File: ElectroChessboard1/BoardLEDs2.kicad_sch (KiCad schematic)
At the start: 35 parts, among them IC73 CD74HC154M96

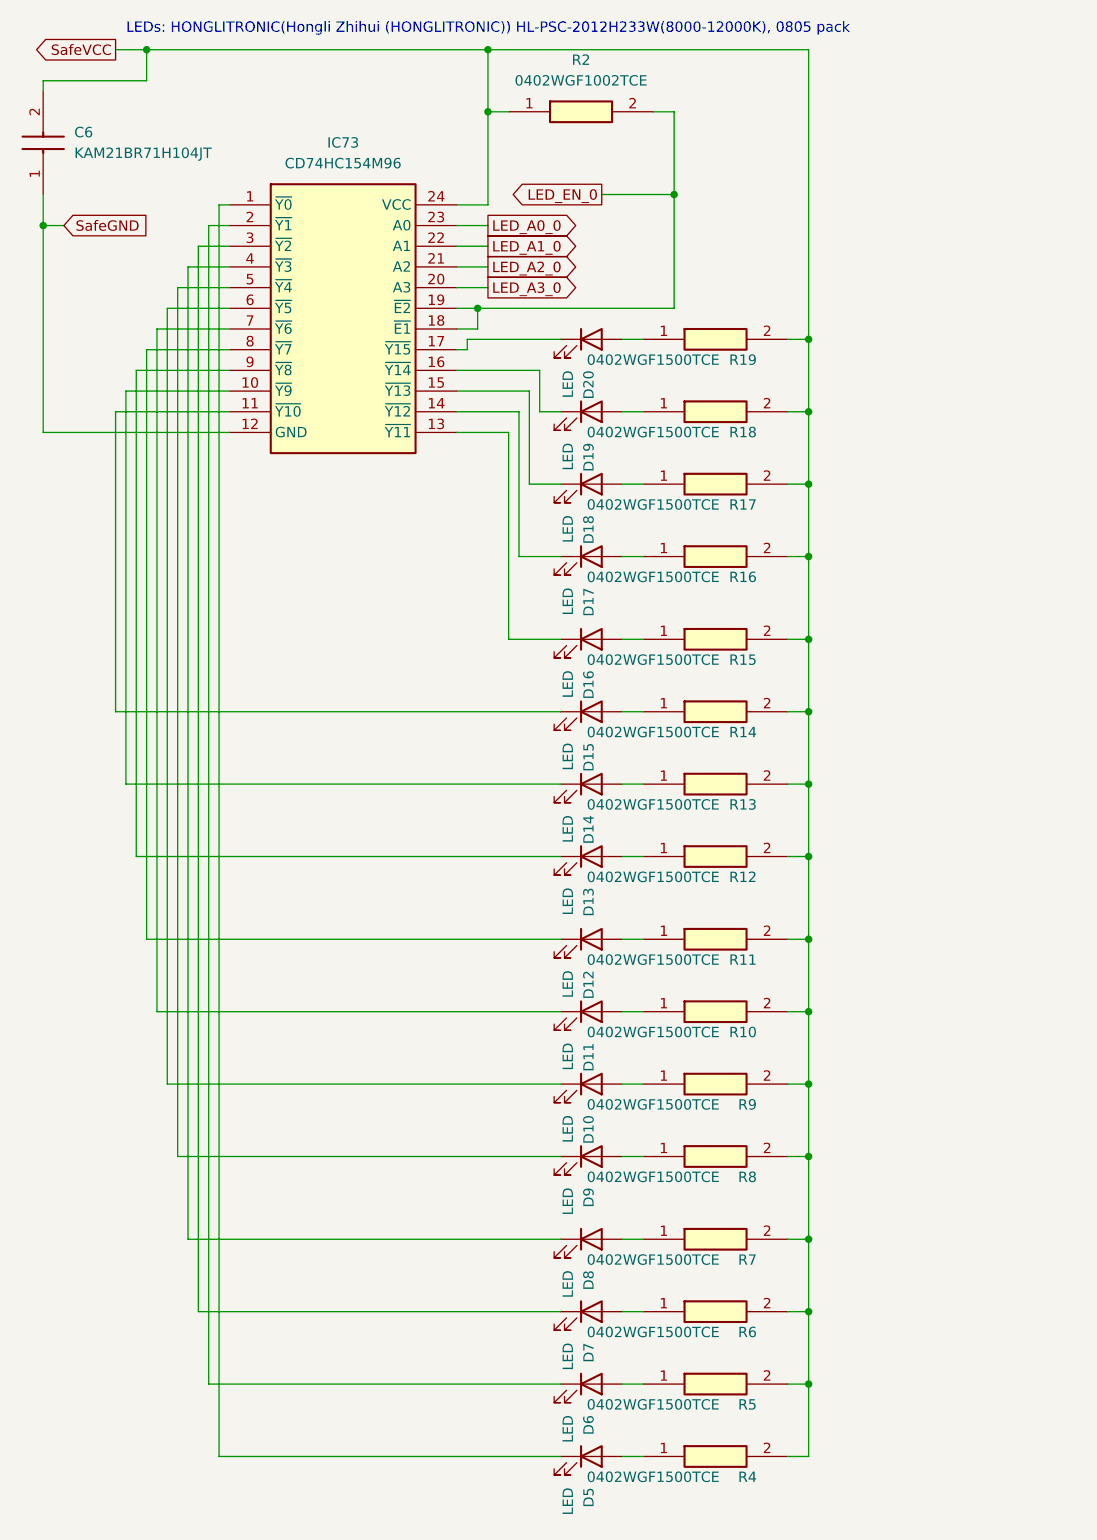
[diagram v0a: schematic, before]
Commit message: LEDs added
Wired Hall sensors and LEDs
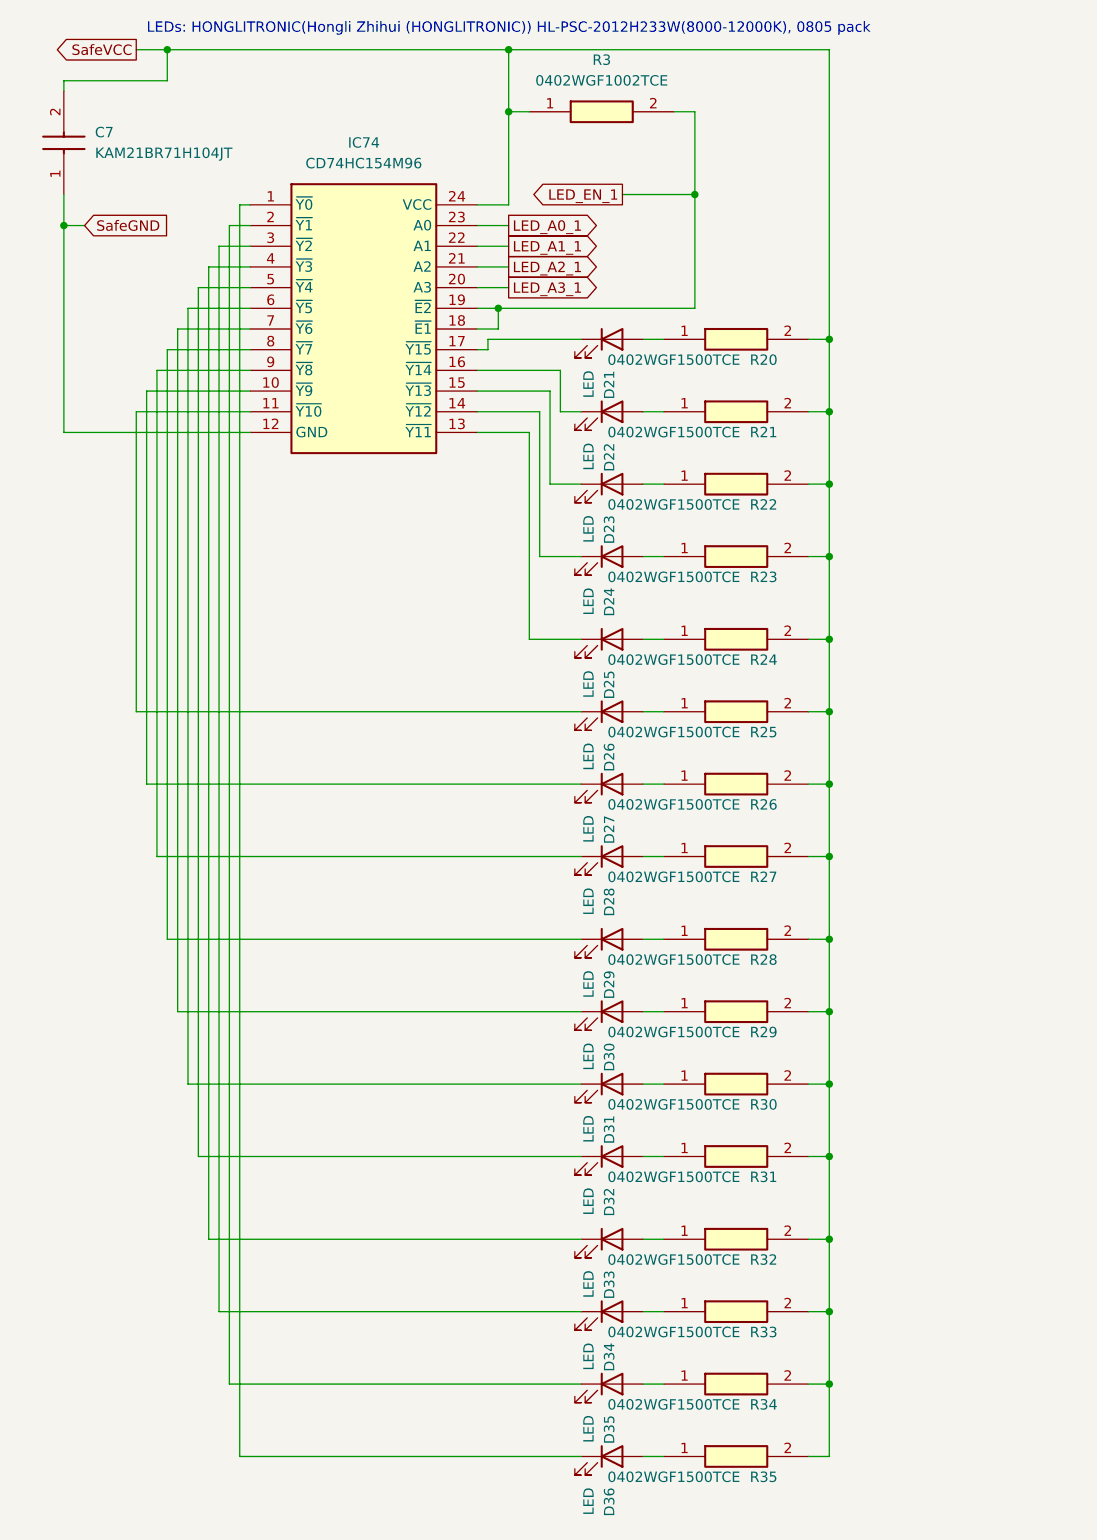
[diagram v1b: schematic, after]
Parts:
- removed C6: KAM21BR71H104JT, CAPC2012X94N, symbol SamacSys_Parts:KAM21BR71H104JT
- removed D10, D11, D12, D13, D14, D15, D16, D17, D18, D19, D20, D5, D6, D7, D8, D9: LED, LED_SMD:LED_0805_2012Metric, symbol Device:LED
- removed IC73: CD74HC154M96, SOIC127P1030X265-24N, symbol SamacSys_Parts:CD74HC154M96
- removed R10, R11, R12, R13, R14, R15, R16, R17, R18, R19, R4, R5, R6, R7, R8, R9: 0402WGF1500TCE, RESC1005X40N, symbol SamacSys_Parts:0402WGF1500TCE
- removed R2: 0402WGF1002TCE, RESC1005X40N, symbol SamacSys_Parts:0402WGF1002TCE
- added C7: KAM21BR71H104JT, CAPC2012X94N, symbol SamacSys_Parts:KAM21BR71H104JT
- added D21, D22, D23, D24, D25, D26, D27, D28, D29, D30, D31, D32, D33, D34, D35, D36: LED, LED_SMD:LED_0805_2012Metric, symbol Device:LED
- added IC74: CD74HC154M96, SOIC127P1030X265-24N, symbol SamacSys_Parts:CD74HC154M96
- added R20, R21, R22, R23, R24, R25, R26, R27, R28, R29, R30, R31, R32, R33, R34, R35: 0402WGF1500TCE, RESC1005X40N, symbol SamacSys_Parts:0402WGF1500TCE
- added R3: 0402WGF1002TCE, RESC1005X40N, symbol SamacSys_Parts:0402WGF1002TCE
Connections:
- net SafeGND: now also C7.1, IC74.12 (GND)
- net SafeVCC: now also C7.2, IC74.24 (VCC), R20.2, R21.2, R22.2, R23.2, R24.2, R25.2, R26.2, R27.2, R28.2, R29.2, R3.1, R30.2, R31.2, R32.2, R33.2, R34.2, R35.2
- new net: D22.1 (K), IC74.16 (~{Y14})
- new net: D22.2 (A), R21.1
- new net: D36.2 (A), R35.1
- new net: D35.2 (A), R34.1
- new net: D31.1 (K), IC74.6 (~{Y5})
- new net: D31.2 (A), R30.1
- new net: D29.1 (K), IC74.8 (~{Y7})
- new net: D29.2 (A), R28.1
- new net: D25.1 (K), IC74.13 (~{Y11})
- new net: D25.2 (A), R24.1
- new net: D21.2 (A), R20.1
- new net: D36.1 (K), IC74.1 (~{Y0})
- new net: D32.1 (K), IC74.5 (~{Y4})
- new net: D32.2 (A), R31.1
- new net: D33.2 (A), R32.1
- new net: D23.1 (K), IC74.15 (~{Y13})
- new net: D23.2 (A), R22.1
- new net: D26.2 (A), R25.1
- new net: D21.1 (K), IC74.17 (~{Y15})
- new net: D26.1 (K), IC74.11 (~{Y10})
- new net: D35.1 (K), IC74.2 (~{Y1})
- new net: D34.2 (A), R33.1
- new net: D28.2 (A), R27.1
- new net: D27.1 (K), IC74.10 (~{Y9})
- new net: D27.2 (A), R26.1
- new net: D24.1 (K), IC74.14 (~{Y12})
- new net: D34.1 (K), IC74.3 (~{Y2})
- new net: D33.1 (K), IC74.4 (~{Y3})
- new net: D30.1 (K), IC74.7 (~{Y6})
- new net: D28.1 (K), IC74.9 (~{Y8})
- new net: D30.2 (A), R29.1
- new net: D24.2 (A), R23.1
- new net LED_A0_1: IC74.23 (A0)
- new net LED_A1_1: IC74.22 (A1)
- new net LED_A2_1: IC74.21 (A2)
- new net LED_A3_1: IC74.20 (A3)
- new net LED_EN_1: IC74.18 (~{E1}), IC74.19 (~{E2}), R3.2

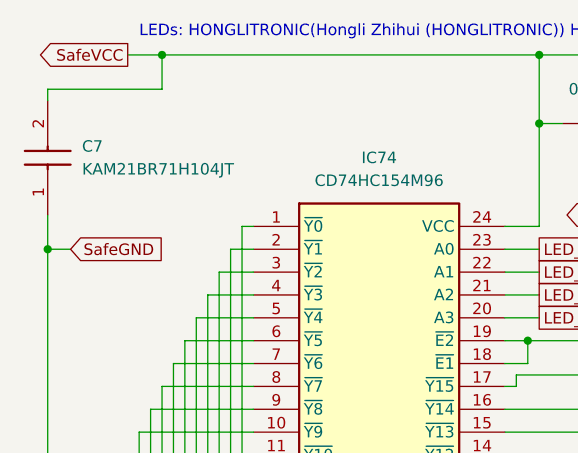
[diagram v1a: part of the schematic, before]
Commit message: Corrected footprints 1
Chosen footprints for JLCPCB
I may add USB insterface chip
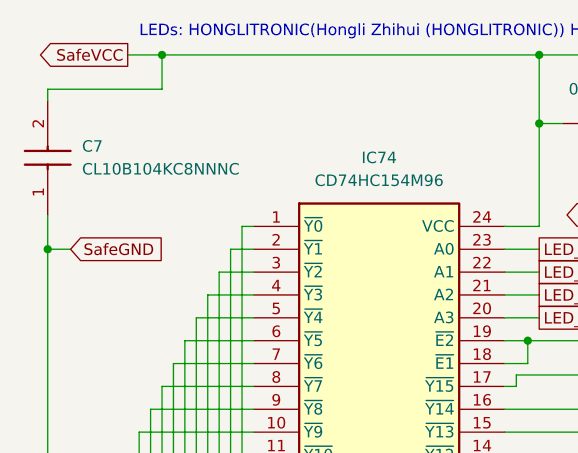
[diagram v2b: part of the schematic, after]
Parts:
- removed C7: KAM21BR71H104JT, CAPC2012X94N, symbol SamacSys_Parts:KAM21BR71H104JT
- added C7: CL10B104KC8NNNC, SamacSys_Parts:CAPC1608X90N, symbol SamacSys_Parts:CL10B104KC8NNNC
- IC74: footprint SOIC127P1030X265-24N -> SamacSys_Parts:SOIC127P1030X265-24N
- R20, R21, R22, R23, R24, R25, R26, R27, R28, R29, R3, R30, R31, R32, R33, R34, R35: footprint RESC1005X40N -> SamacSys_Parts:RESC1005X40N
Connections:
- net SafeGND: now also C7.1
- net SafeVCC: now also C7.2
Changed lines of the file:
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@@
 			)
 		)
-		(property "Footprint" "RESC1005X40N"
+		(property "Footprint" "SamacSys_Parts:RESC1005X40N"
 			(at 106.68 285.42 0)
 			(effects
@@
 			)
 		)
-		(property "Footprint" "RESC1005X40N"
+		(property "Footprint" "SamacSys_Parts:RESC1005X40N"
 			(at 106.68 276.53 0)
 			(effects
@@
 			)
 		)
-		(property "Footprint" "RESC1005X40N"
+		(property "Footprint" "SamacSys_Parts:RESC1005X40N"
 			(at 106.68 148.26 0)
 			(effects
@@
 			)
 		)
-		(property "Footprint" "RESC1005X40N"
+		(property "Footprint" "SamacSys_Parts:RESC1005X40N"
 			(at 106.68 239.7 0)
 			(effects
@@
 			)
 		)
-		(property "Footprint" "RESC1005X40N"
+		(property "Footprint" "SamacSys_Parts:RESC1005X40N"
 			(at 106.68 258.75 0)
 			(effects
@@
 	)
 	(symbol
-		(lib_id "SamacSys_Parts:KAM21BR71H104JT")
+		(lib_id "SamacSys_Parts:CL10B104KC8NNNC")
 		(at 19.05 34.29 90)
 		(unit 1)
@@
 			)
 		)
-		(property "Value" "KAM21BR71H104JT"
+		(property "Value" "CL10B104KC8NNNC"
 			(at 22.86 29.2099 90)
 			(effects
@@
 			)
 		)
-		(property "Footprint" "CAPC2012X94N"
+		(property "Footprint" "SamacSys_Parts:CAPC1608X90N"
 			(at 115.24 25.4 0)
 			(effects
@@
 			)
 		)
-		(property "Datasheet" "https://spicat.kyocera-avx.com/product/mlcc/chartview/KAM21BR71H104JT/DataSheet/X7R"
+		(property "Datasheet" "https://datasheet.datasheetarchive.com/originals/distributors/DKDS-19/373511.pdf"
 			(at 215.24 25.4 0)
 			(effects
@@
 			)
 		)
-		(property "Description" "Multilayer Ceramic Capacitors MLCC - SMD/SMT 50V .1uF X7R 0805 5% AEC-Q200"
+		(property "Description" "Samsung"
 			(at 19.05 34.29 0)
 			(effects
@@
 			)
 		)
-		(property "Height" "0.94"
+		(property "Height" "0.9"
 			(at 415.24 25.4 0)
 			(effects
@@
 			)
 		)
-		(property "Mouser Part Number" "581-KAM21BR71H104JT"
+		(property "Mouser Part Number" "187-CL10B104KC8NNNC"
 			(at 515.24 25.4 0)
 			(effects
@@
 			)
 		)
-		(property "Mouser Price/Stock" "https://www.mouser.co.uk/ProductDetail/KYOCERA-AVX/KAM21BR71H104JT?qs=Jm2GQyTW%2Fbic6Zk4McEt6w%3D%3D"
+		(property "Mouser Price/Stock" "https://www.mouser.co.uk/ProductDetail/Samsung-Electro-Mechanics/CL10B104KC8NNNC?qs=%2FukktrhNKsY5bKXvqblW4Q%3D%3D"
 			(at 615.24 25.4 0)
 			(effects
@@
 			)
 		)
-		(property "Manufacturer_Name" "Kyocera AVX"
+		(property "Manufacturer_Name" "SAMSUNG"
 			(at 715.24 25.4 0)
 			(effects
@@
 			)
 		)
-		(property "Manufacturer_Part_Number" "KAM21BR71H104JT"
+		(property "Manufacturer_Part_Number" "CL10B104KC8NNNC"
 			(at 815.24 25.4 0)
 			(effects
@@
 			)
 		)
-		(pin "1"
-		)
 		(pin "2"
 		)
+		(pin "1"
+		)
 		(instances
 			(project "ElectroChessboard1"
@@
 			)
 		)
-		(property "Footprint" "RESC1005X40N"
+		(property "Footprint" "SamacSys_Parts:RESC1005X40N"
 			(at 106.68 221.92 0)
 			(effects
@@
 			)
 		)
-		(property "Footprint" "RESC1005X40N"
+		(property "Footprint" "SamacSys_Parts:RESC1005X40N"
 			(at 106.68 193.98 0)
 			(effects
@@
 			)
 		)
-		(property "Footprint" "RESC1005X40N"
+		(property "Footprint" "SamacSys_Parts:RESC1005X40N"
 			(at 90.17 120.32 0)
 			(effects
@@
 			)
 		)
-		(property "Footprint" "RESC1005X40N"
+		(property "Footprint" "SamacSys_Parts:RESC1005X40N"
 			(at 106.68 267.64 0)
 			(effects
@@
 			)
 		)
-		(property "Footprint" "RESC1005X40N"
+		(property "Footprint" "SamacSys_Parts:RESC1005X40N"
 			(at 106.68 211.76 0)
 			(effects
@@
 			)
 		)
-		(property "Footprint" "SOIC127P1030X265-24N"
+		(property "Footprint" "SamacSys_Parts:SOIC127P1030X265-24N"
 			(at 66.04 130.48 0)
 			(effects
@@
 			)
 		)
-		(property "Footprint" "RESC1005X40N"
+		(property "Footprint" "SamacSys_Parts:RESC1005X40N"
 			(at 106.68 230.81 0)
 			(effects
@@
 			)
 		)
-		(property "Footprint" "RESC1005X40N"
+		(property "Footprint" "SamacSys_Parts:RESC1005X40N"
 			(at 106.68 248.59 0)
 			(effects
@@
 			)
 		)
-		(property "Footprint" "RESC1005X40N"
+		(property "Footprint" "SamacSys_Parts:RESC1005X40N"
 			(at 106.68 166.04 0)
 			(effects
@@
 			)
 		)
-		(property "Footprint" "RESC1005X40N"
+		(property "Footprint" "SamacSys_Parts:RESC1005X40N"
 			(at 106.68 174.93 0)
 			(effects
@@
 			)
 		)
-		(property "Footprint" "RESC1005X40N"
+		(property "Footprint" "SamacSys_Parts:RESC1005X40N"
 			(at 106.68 185.09 0)
 			(effects
@@
 			)
 		)
-		(property "Footprint" "RESC1005X40N"
+		(property "Footprint" "SamacSys_Parts:RESC1005X40N"
 			(at 106.68 157.15 0)
 			(effects
@@
 			)
 		)
-		(property "Footprint" "RESC1005X40N"
+		(property "Footprint" "SamacSys_Parts:RESC1005X40N"
 			(at 106.68 202.87 0)
 			(effects
